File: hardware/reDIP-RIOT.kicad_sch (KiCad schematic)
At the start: 31 parts, among them J1 Conn_01x20, J2 Conn_01x20, J3 Conn_02x05_Odd_Even, U1 NCP115AMX120TCG, U2 NCP115AMX330TCG, U3 SN74CBT16210CDGGR, U4 SN74CBT16210CDGGR, U5 74AHCT1G14, U6 ICE5LP1K-SG48, U7 AT25EU0011A-SSHN

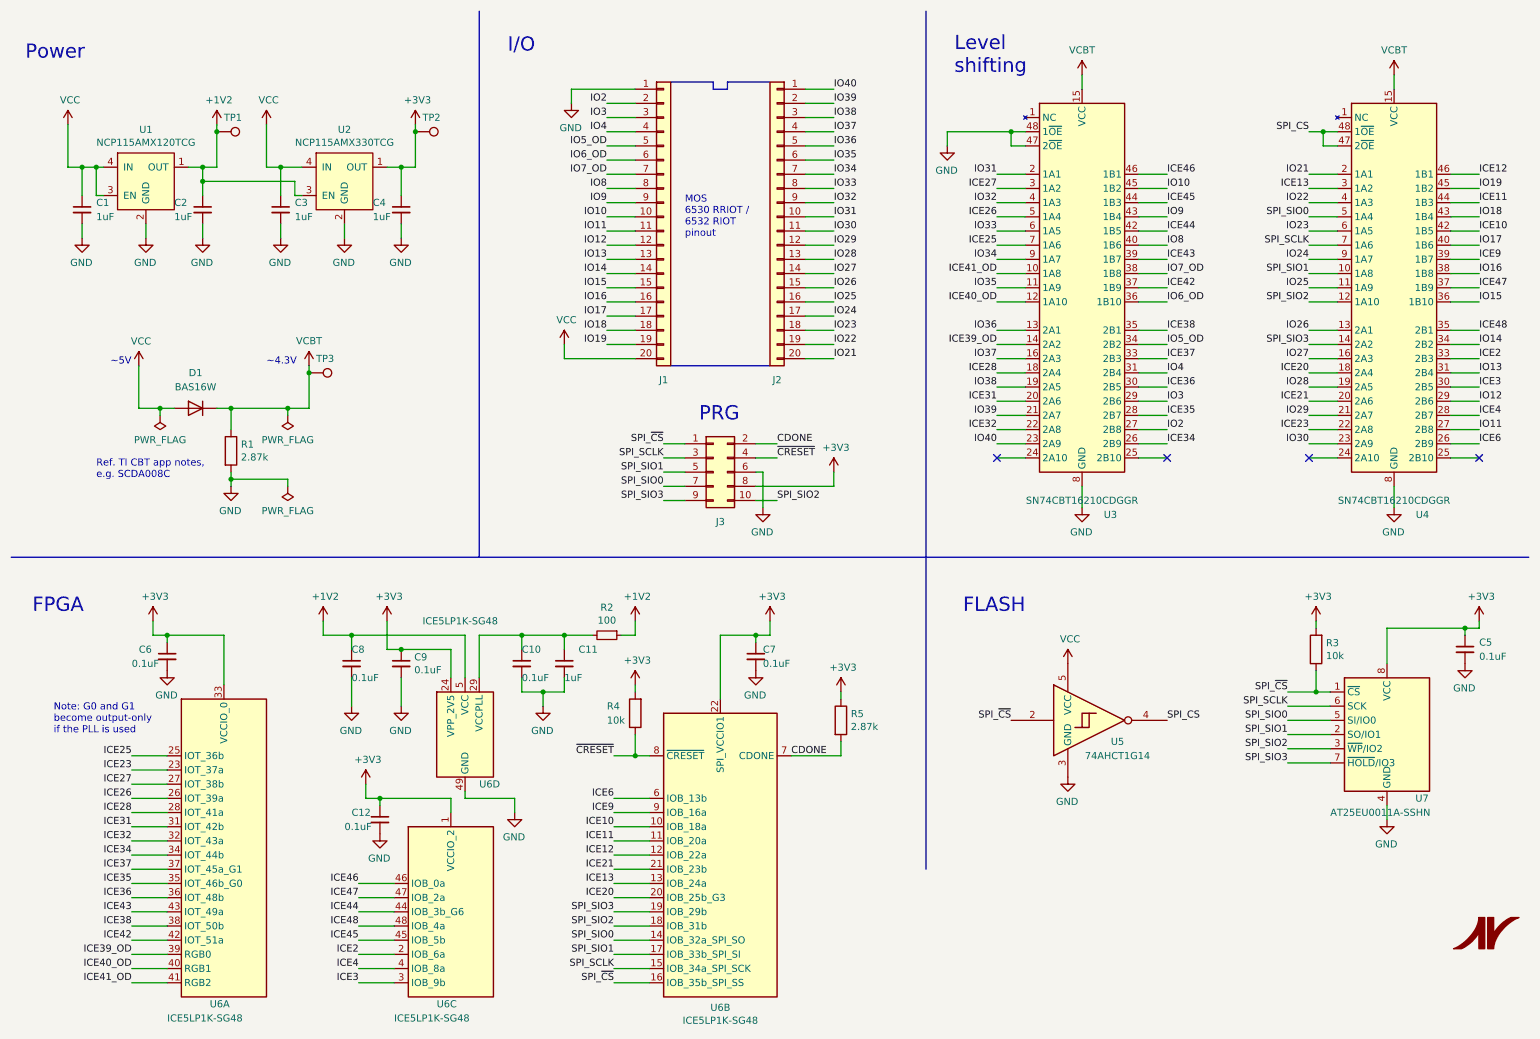
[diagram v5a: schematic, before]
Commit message: Replaced iCE5LP1K with iCE40UP5K
The MOS 6530 and MOS 6532 have on-chip data port pull-up resistors
in the range of 5k.

While the iCE40UP5K features configurable 3.3k/6.8k/10k/100k pull-up
resistors, the iCE5LP1K only features 100k pull-up resistors.

We make the simple fix of using the more capable (and somewhat more
expensive) pin compatible iCE40UP5K, instead of adding physical
pull-up resistors to separate boards for the MOS 6530 and MOS 6532.
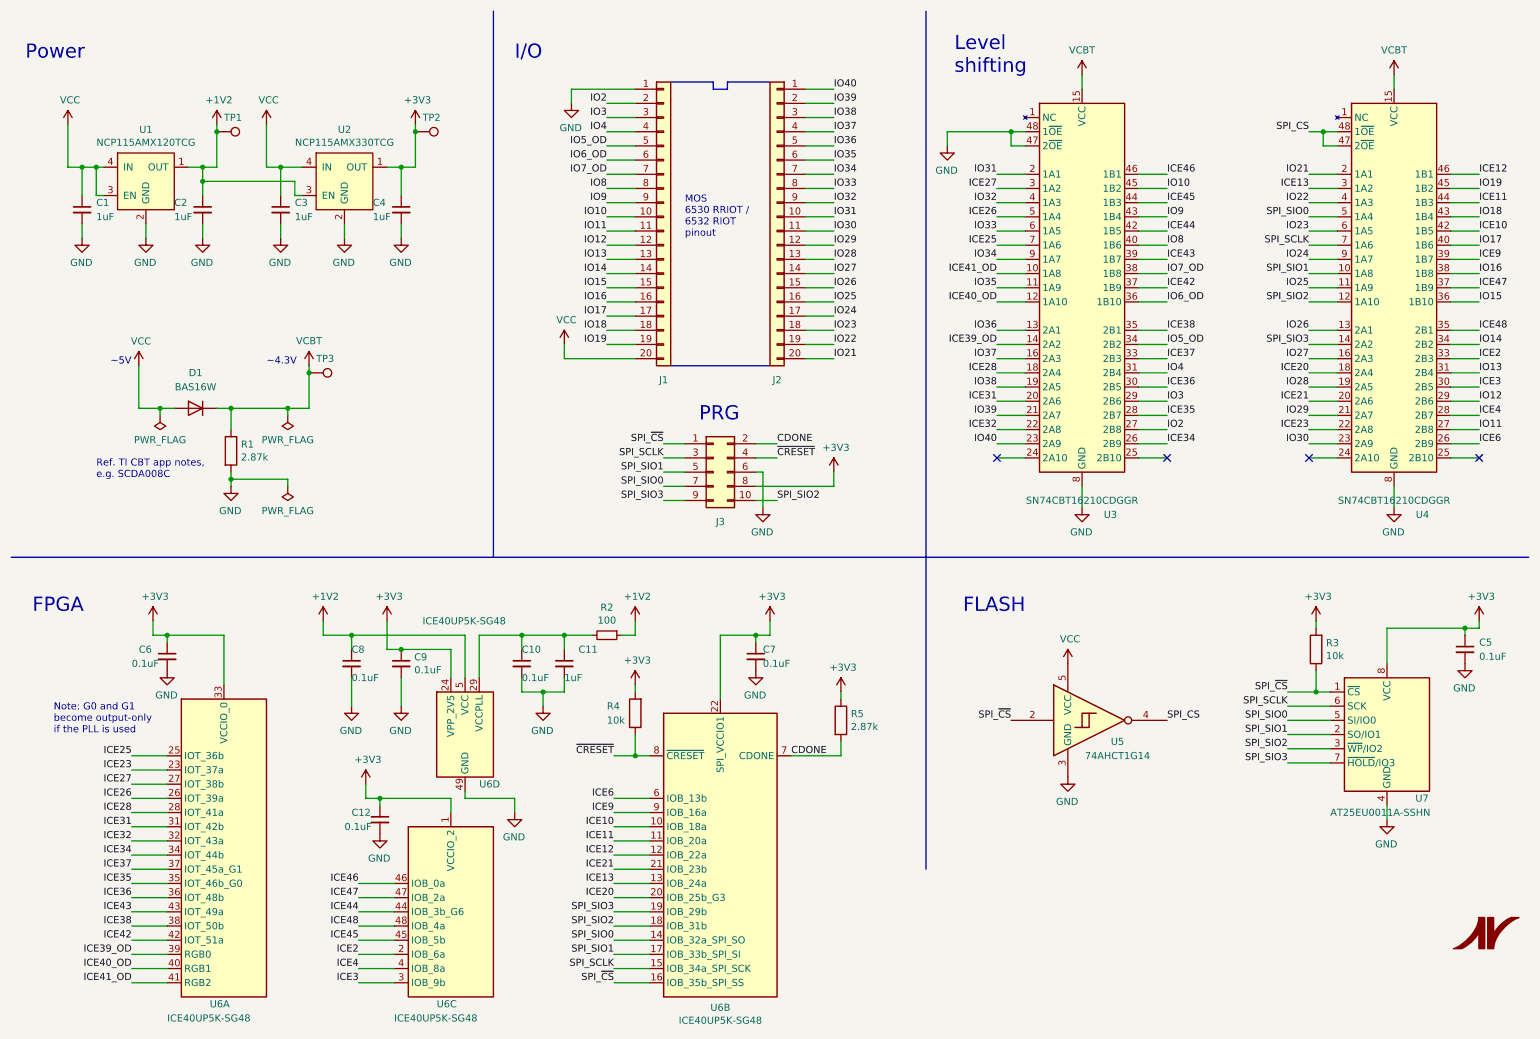
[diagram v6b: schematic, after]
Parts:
- U6: value ICE5LP1K-SG48 -> ICE40UP5K-SG48; symbol FPGA_Lattice:ICE5LP1K-SG48 -> FPGA_Lattice:ICE40UP5K-SG48ITR; PN ICE5LP1K-SG48ITR -> ICE40UP5K-SG48I
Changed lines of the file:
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@@
     (stroke (width 0) (type default))
   )
-  (polyline (pts (xy 96.52 12.7) (xy 96.52 110.49))
+  (polyline (pts (xy 99.06 12.7) (xy 99.06 110.49))
     (stroke (width 0) (type default))
   )
@@
     (effects (font (size 2.54 2.54)) (justify left bottom))
   )
-  (text "I/O" (at 101.6 20.32 0)
+  (text "I/O" (at 102.87 21.59 0)
     (effects (font (size 2.54 2.54)) (justify left bottom))
   )
@@
     (effects (font (size 1.27 1.27)) (justify left bottom))
   )
-  (symbol (lib_id "FPGA_Lattice:ICE5LP1K-SG48") (at 50.8 161.29 0) (unit 1)
+  (symbol (lib_id "FPGA_Lattice:ICE40UP5K-SG48ITR") (at 50.8 161.29 0) (unit 1)
     (in_bom yes) (on_board yes) (dnp no)
     (property "Reference" "U6" (at 48.26 190.5 0)
       (effects (font (size 1.27 1.27)) (justify left))
     )
-    (property "Value" "ICE5LP1K-SG48" (at 40.64 193.04 0)
+    (property "Value" "ICE40UP5K-SG48" (at 40.64 193.04 0)
       (effects (font (size 1.27 1.27)) (justify left))
     )
@@
       (effects (font (size 1.27 1.27)) hide)
     )
-    (property "Datasheet" "https://www.latticesemi.com/Products/FPGAandCPLD/iCE40" (at 40.64 135.89 0)
+    (property "Datasheet" "http://www.latticesemi.com/Products/FPGAandCPLD/iCE40Ultra" (at 40.64 135.89 0)
       (effects (font (size 1.27 1.27)) hide)
     )
@@
       (effects (font (size 1.27 1.27)) hide)
     )
-    (property "PN" "ICE5LP1K-SG48ITR" (at 50.8 161.29 0)
+    (property "PN" "ICE40UP5K-SG48I" (at 50.8 161.29 0)
       (effects (font (size 1.27 1.27)) hide)
     )
@@
     )
   )
-  (symbol (lib_id "FPGA_Lattice:ICE5LP1K-SG48") (at 139.7 163.83 0) (unit 2)
+  (symbol (lib_id "FPGA_Lattice:ICE40UP5K-SG48ITR") (at 139.7 163.83 0) (unit 2)
     (in_bom yes) (on_board yes) (dnp no)
     (property "Reference" "U6" (at 139.7 191.135 0)
       (effects (font (size 1.27 1.27)))
     )
-    (property "Value" "ICE5LP1K-SG48" (at 139.7 193.4464 0)
+    (property "Value" "ICE40UP5K-SG48" (at 139.7 193.4464 0)
       (effects (font (size 1.27 1.27)))
     )
@@
       (effects (font (size 1.27 1.27)) hide)
     )
-    (property "Datasheet" "https://www.latticesemi.com/Products/FPGAandCPLD/iCE40" (at 129.54 138.43 0)
+    (property "Datasheet" "http://www.latticesemi.com/Products/FPGAandCPLD/iCE40Ultra" (at 129.54 138.43 0)
       (effects (font (size 1.27 1.27)) hide)
     )
@@
       (effects (font (size 1.27 1.27)) hide)
     )
-    (property "PN" "ICE5LP1K-SG48ITR" (at 139.7 163.83 0)
+    (property "PN" "ICE40UP5K-SG48I" (at 139.7 163.83 0)
       (effects (font (size 1.27 1.27)) hide)
     )
@@
     )
   )
-  (symbol (lib_id "FPGA_Lattice:ICE5LP1K-SG48") (at 91.44 173.99 0) (unit 3)
+  (symbol (lib_id "FPGA_Lattice:ICE40UP5K-SG48ITR") (at 91.44 173.99 0) (unit 3)
     (in_bom yes) (on_board yes) (dnp no)
     (property "Reference" "U6" (at 88.9 190.5 0)
       (effects (font (size 1.27 1.27)) (justify left))
     )
-    (property "Value" "ICE5LP1K-SG48" (at 81.28 193.04 0)
+    (property "Value" "ICE40UP5K-SG48" (at 81.28 193.04 0)
       (effects (font (size 1.27 1.27)) (justify left))
     )
@@
       (effects (font (size 1.27 1.27)) hide)
     )
-    (property "Datasheet" "https://www.latticesemi.com/Products/FPGAandCPLD/iCE40" (at 81.28 148.59 0)
+    (property "Datasheet" "http://www.latticesemi.com/Products/FPGAandCPLD/iCE40Ultra" (at 81.28 148.59 0)
       (effects (font (size 1.27 1.27)) hide)
     )
@@
       (effects (font (size 1.27 1.27)) hide)
     )
-    (property "PN" "ICE5LP1K-SG48ITR" (at 91.44 173.99 0)
+    (property "PN" "ICE40UP5K-SG48I" (at 91.44 173.99 0)
       (effects (font (size 1.27 1.27)) hide)
     )
@@
     )
   )
-  (symbol (lib_id "FPGA_Lattice:ICE5LP1K-SG48") (at 93.98 142.24 0) (unit 4)
+  (symbol (lib_id "FPGA_Lattice:ICE40UP5K-SG48ITR") (at 93.98 142.24 0) (unit 4)
     (in_bom yes) (on_board yes) (dnp no)
     (property "Reference" "U6" (at 96.52 151.13 0)
       (effects (font (size 1.27 1.27)) (justify left))
     )
-    (property "Value" "ICE5LP1K-SG48" (at 86.36 121.92 0)
+    (property "Value" "ICE40UP5K-SG48" (at 86.36 121.92 0)
       (effects (font (size 1.27 1.27)) (justify left))
     )
@@
       (effects (font (size 1.27 1.27)) hide)
     )
-    (property "Datasheet" "https://www.latticesemi.com/Products/FPGAandCPLD/iCE40" (at 83.82 116.84 0)
+    (property "Datasheet" "http://www.latticesemi.com/Products/FPGAandCPLD/iCE40Ultra" (at 83.82 116.84 0)
       (effects (font (size 1.27 1.27)) hide)
     )
@@
       (effects (font (size 1.27 1.27)) hide)
     )
-    (property "PN" "ICE5LP1K-SG48ITR" (at 93.98 142.24 0)
+    (property "PN" "ICE40UP5K-SG48I" (at 93.98 142.24 0)
       (effects (font (size 1.27 1.27)) hide)
     )
@@
   (symbol (lib_id "power:VCC") (at 201.93 129.54 0) (unit 1)
     (in_bom yes) (on_board yes) (dnp no)
-    (property "Reference" "#PWR044" (at 201.93 133.35 0)
+    (property "Reference" "#PWR030" (at 201.93 133.35 0)
       (effects (font (size 1.27 1.27)) hide)
     )
@@
       (project "reDIP-RIOT"
         (path "/34d03349-6d78-4165-a683-2d8b76f2bae8"
-          (reference "#PWR044") (unit 1)
+          (reference "#PWR030") (unit 1)
         )
       )
